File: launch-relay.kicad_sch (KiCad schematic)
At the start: 0 parts

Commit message: started schematic
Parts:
- added U1: (no value), RF_Module:BM78SPPS5XC2, symbol HPRC_Sensors:BMA580
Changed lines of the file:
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@@
 	(generator_version "10.0")
 	(paper "A4")
+	(symbol
+		(lib_id "HPRC_Sensors:BMA580")
+		(at 48.26 167.64 0)
+		(unit 1)
+		(body_style 1)
+		(exclude_from_sim no)
+		(in_bom yes)
+		(on_board yes)
+		(in_pos_files yes)
+		(dnp no)
+		(fields_autoplaced yes)
+		(property "Reference" "U1"
+			(at 48.26 157.48 0)
+			(show_name no)
+			(do_not_autoplace no)
+			(effects
+				(font
+					(size 1.27 1.27)
+				)
+			)
+		)
+		(property "Value" ""
+			(at 48.26 167.64 0)
+			(show_name no)
+			(do_not_autoplace no)
+			(effects
+				(font
+					(size 1.27 1.27)
+				)
+			)
+		)
+		(property "Footprint" "RF_Module:BM78SPPS5XC2"
+			(at 48.26 167.64 0)
+			(hide yes)
+			(show_name no)
+			(do_not_autoplace no)
+			(effects
+				(font
+					(size 1.27 1.27)
+				)
+			)
+		)
+		(property "Datasheet" ""
+			(at 48.26 167.64 0)
+			(hide yes)
+			(show_name no)
+			(do_not_autoplace no)
+			(effects
+				(font
+					(size 1.27 1.27)
+				)
+			)
+		)
+		(property "Description" ""
+			(at 48.26 167.64 0)
+			(hide yes)
+			(show_name no)
+			(do_not_autoplace no)
+			(effects
+				(font
+					(size 1.27 1.27)
+				)
+			)
+		)
+		(pin "1"
+		)
+		(pin "6"
+		)
+		(pin "4"
+		)
+		(pin "3"
+		)
+		(pin "2"
+		)
+		(pin "5"
+		)
+		(instances
+			(project "launch-relay"
+				(path "/5fd10500-b703-4d79-824f-0c6e126f5ac0"
+					(reference "U1")
+					(unit 1)
+				)
+			)
+		)
+	)
 	(sheet_instances
 		(path "/"

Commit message: started schematic
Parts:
- removed U1: (no value), RF_Module:BM78SPPS5XC2, symbol HPRC_Sensors:BMA580
- added BT1: BHSD-2032-PC, BHSD-2032-PC:BAT_BHSD-2032-PC, symbol BHSD-2032-PC:BHSD-2032-PC
- added C1: 100nF, symbol Device:C
- added D1, D2: LED, symbol Device:LED
- added J1: Conn_01x05_Pin, Package_DFN_QFN:QFN-20-1EP_5x5mm_P0.65mm_EP3.35x3.35mm, symbol Connector:Conn_01x05_Pin
- added R1, R2, R3, R4: 2.2k, symbol Device:R
- added U1: STM32U083KCUx, Package_DFN_QFN:QFN-32-1EP_5x5mm_P0.5mm_EP3.45x3.45mm, symbol MCU_ST_STM32U0:STM32U083KCUx
- added U3: (no value), RF_Module:BM78SPPS5XC2, symbol HPRC_Sensors:BMA580
- added U5: MX25R3235FM1IL0, SOP_8L_150_MAC, symbol MX25R3235FM1IL0:MX25R3235FM1IL0
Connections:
- new net: D1.2 (A), R3.2
- new net: D2.2 (A), R4.2
- new net +3V0: BT1.S+1, BT1.S+2, R1.2, R2.2, U1.1 (VDD), U1.17 (VDD), U1.5 (VDDA), U3.6 (VSS), U5.8 (VCC)
- new net BMA580_INT: U1.14 (PB0), U3.2 (INT)
- new net Battery_ADC: U1.9 (PA3)
- new net DEBUG_JTCK-SWCLK: U1.24 (PA14)
- new net DEBUG_JTCK_SWCLK: J1.1 (Pin_1)
- new net DEBUG_JTMS-SWDIO: J1.2 (Pin_2), U1.23 (PA13)
- new net DUMP: J1.5 (Pin_5), U1.18 (PA8)
- new net Flash_CS: U1.29 (PB6), U5.1 (CS#)
- new net GND: BT1.-, C1.1, U1.16 (VSS), U1.32 (VSS), U1.33 (VSS), U3.1 (VDD), U5.4 (GND)
- new net I2C2_SCL: R1.1, U1.13 (PA7), U3.5 (SCL)
- new net I2C2_SDA: R2.1, U1.12 (PA6), U3.4 (SDA)
- new net LED1: R4.1, U1.22 (PA12)
- new net LED2: R3.1, U1.21 (PA11)
- new net SPI3_MISO: U1.27 (PB4), U5.2 (SO/SIO1)
- new net SPI3_MOSI: U1.28 (PB5), U5.5 (SI/SIO0)
- new net SPI3_SCK: U1.26 (PB3), U5.6 (SCLK)
- new net Switch1: U1.7 (PA1)
- new net Switch2: U1.8 (PA2)
- new net USART1_RX: J1.3 (Pin_3), U1.20 (PA10)
- new net USART1_TX: J1.4 (Pin_4), U1.19 (PA9)
- new net VDD: U3.3 (INT2)
- no-connect marks 0 -> 9

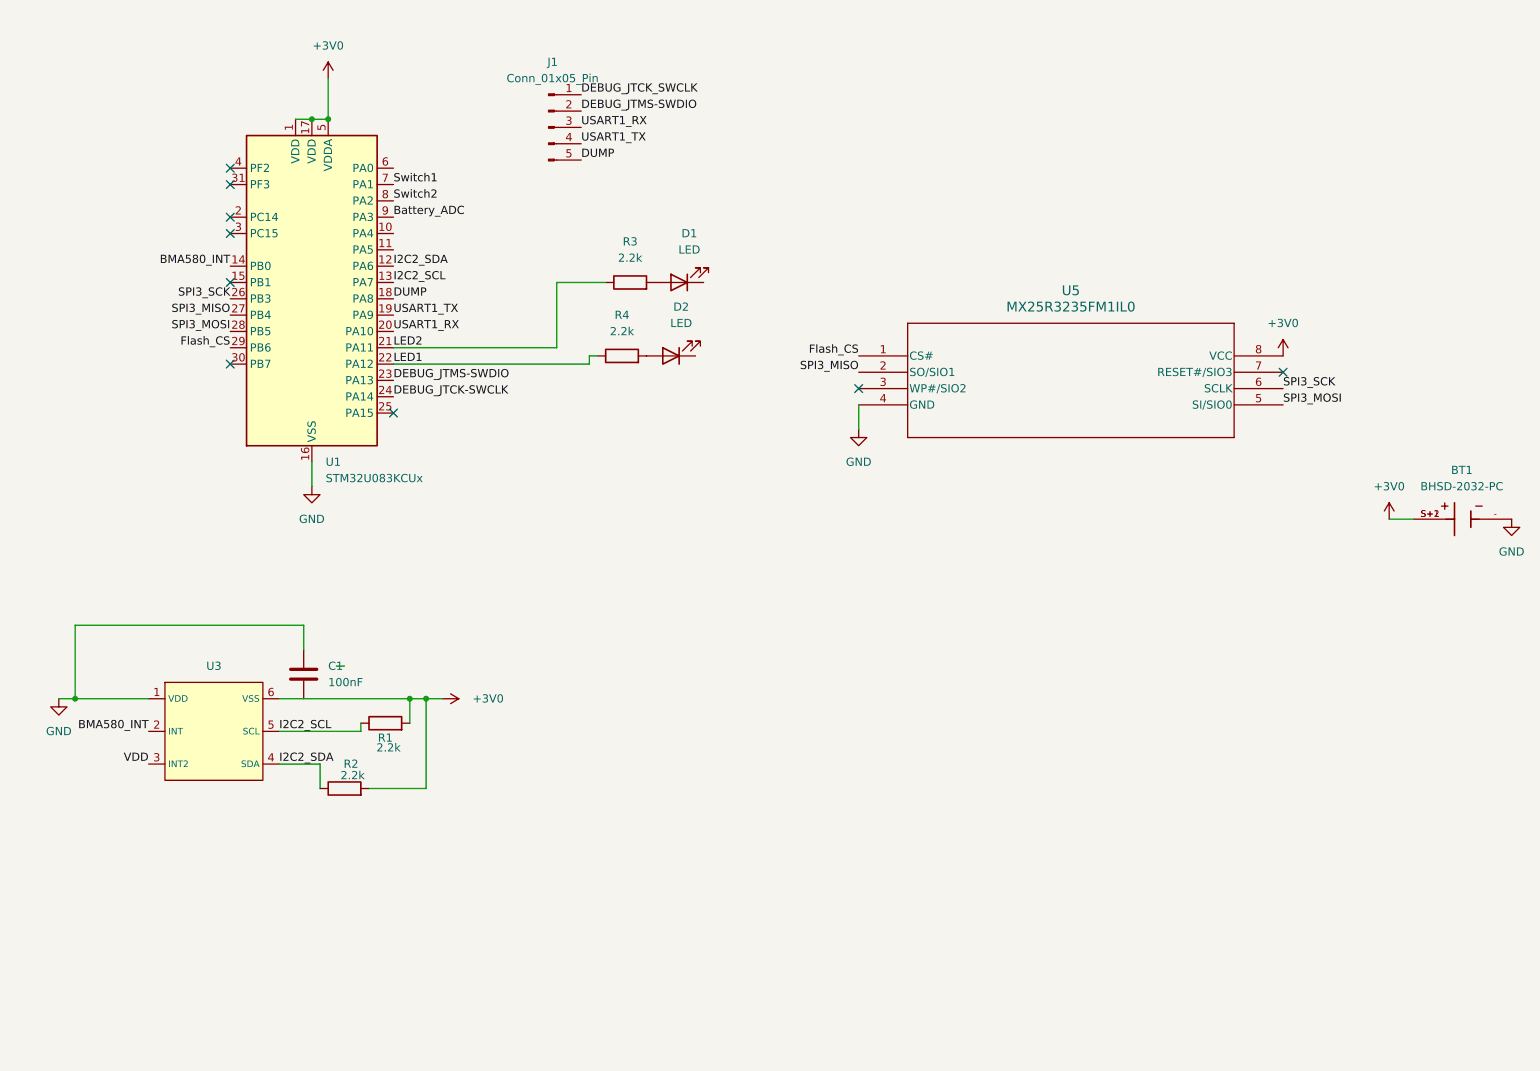
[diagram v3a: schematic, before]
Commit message: finalized schematic and prepped layout
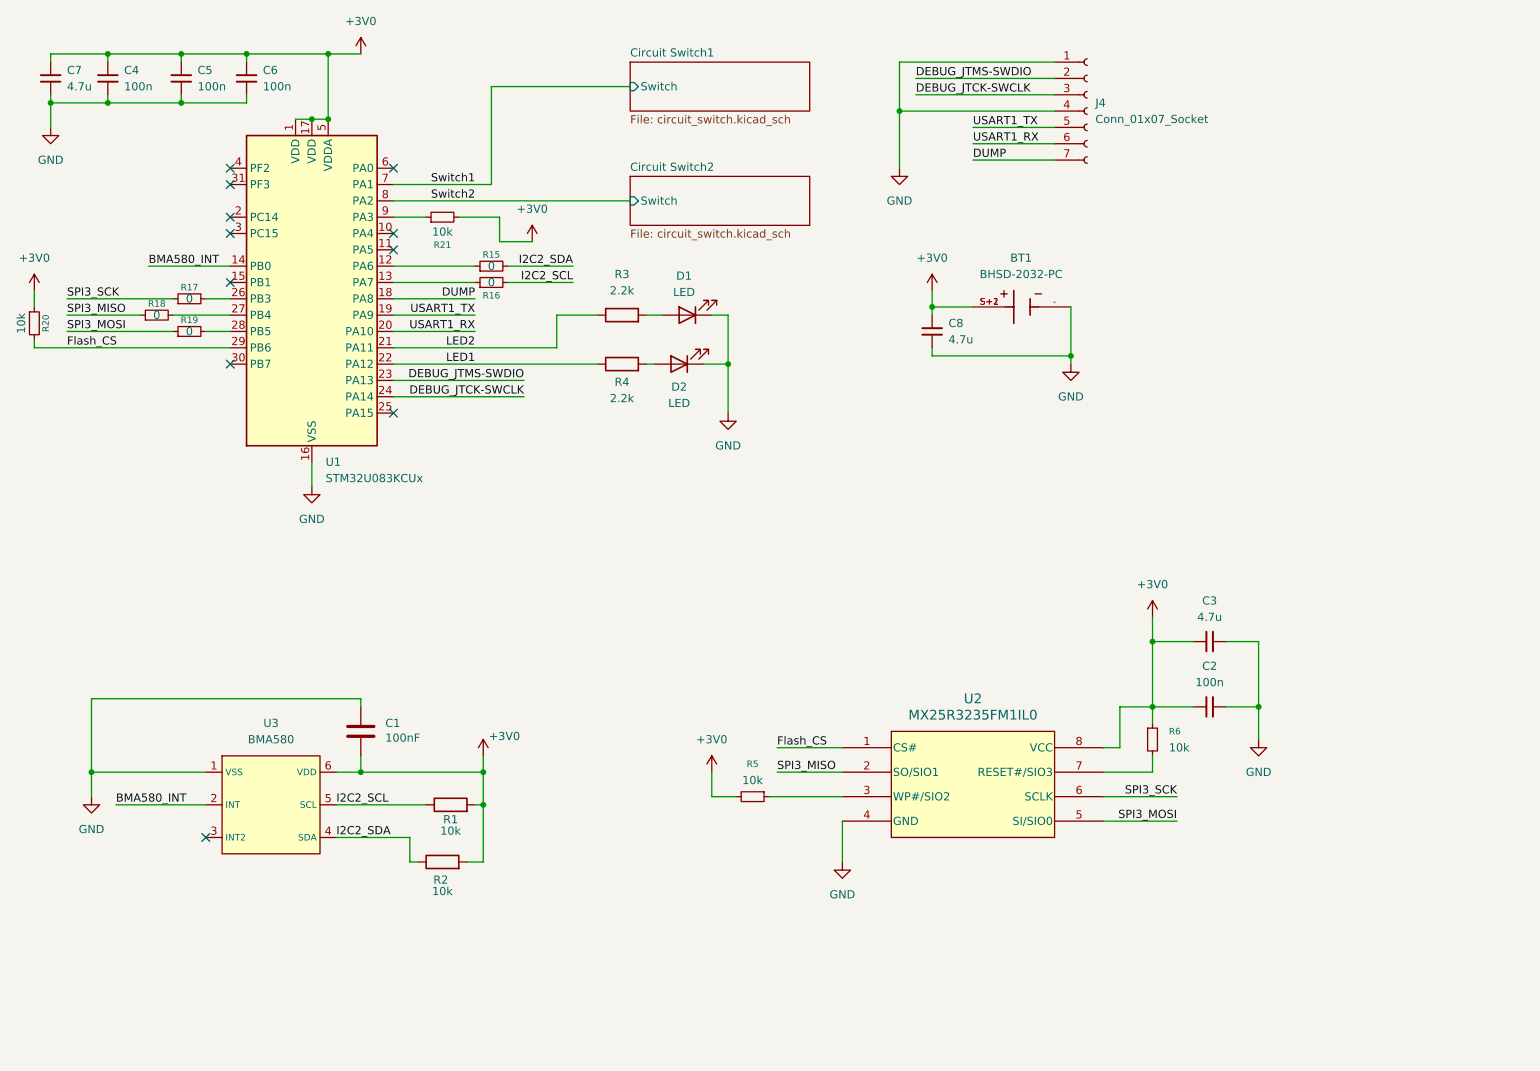
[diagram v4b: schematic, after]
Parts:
- removed J1: Conn_01x05_Pin, Package_DFN_QFN:QFN-20-1EP_5x5mm_P0.65mm_EP3.35x3.35mm, symbol Connector:Conn_01x05_Pin
- removed U5: MX25R3235FM1IL0, SOP_8L_150_MAC, symbol MX25R3235FM1IL0:MX25R3235FM1IL0
- added C2, C4, C5, C6: 100n, Capacitor_SMD:C_0603_1608Metric, symbol Device:C_Small
- added C3, C7, C8: 4.7u, Capacitor_SMD:C_0603_1608Metric, symbol Device:C_Small
- added J4: Conn_01x07_Socket, Connector_PinSocket_2.54mm:PinSocket_1x07_P2.54mm_Vertical, symbol Connector:Conn_01x07_Socket
- added R15, R16, R17, R18, R19: 0, Resistor_SMD:R_0603_1608Metric, symbol Device:R_Small
- added R20, R21, R5, R6: 10k, Resistor_SMD:R_0603_1608Metric, symbol Device:R_Small
- added U2: MX25R3235FM1IL0, HPRC_Storage:SOP_8L_150_MAC, symbol MX25R3235FM1IL0:MX25R3235FM1IL0
- BT1: footprint BHSD-2032-PC:BAT_BHSD-2032-PC -> HPRC_Connectors:BAT_BHSD-2032-PC
- C1: footprint (none) -> Capacitor_SMD:C_0603_1608Metric
- D1, D2: footprint (none) -> LED_SMD:LED_0805_2012Metric
- R1, R2: value 2.2k -> 10k; footprint (none) -> Resistor_SMD:R_0603_1608Metric
- R3, R4: footprint (none) -> Resistor_SMD:R_0603_1608Metric
- U3: value (none) -> BMA580; footprint RF_Module:BM78SPPS5XC2 -> HPRC_Sensors:BMA580
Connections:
- net +3V0: now also C1.2, C2.1, C3.1, C4.2, C5.2, C6.2, C7.2, C8.2, R20.1, R21.2, R5.2, R6.1, U2.8 (VCC)
- net DEBUG_JTCK-SWCLK: now also J4.3 (Pin_3)
- net DEBUG_JTMS-SWDIO: now also J4.2 (Pin_2)
- net DUMP: now also J4.7 (Pin_7)
- net Flash_CS: now also R20.2, U2.1 (CS#)
- net GND: now also D1.1 (K), D2.1 (K), C2.2, C3.2, C4.1, C5.1, C6.1, C7.1, C8.1, J4.1 (Pin_1), J4.4 (Pin_4), U2.4 (GND)
- net I2C2_SCL: now also R16.2; no longer U1.13 (PA7)
- net I2C2_SDA: now also R15.2; no longer U1.12 (PA6)
- net SPI3_MISO: now also R18.1, U2.2 (SO/SIO1); no longer U1.27 (PB4)
- net SPI3_MOSI: now also R19.1, U2.5 (SI/SIO0); no longer U1.28 (PB5)
- net SPI3_SCK: now also R17.1, U2.6 (SCLK); no longer U1.26 (PB3)
- net USART1_RX: now also J4.6 (Pin_6)
- net USART1_TX: now also J4.5 (Pin_5)
- net Battery_ADC: no longer names the net of U1.9 (PA3)
- net Battery_ADC: now also R21.1
- net VDD: no longer names the net of U3.3 (INT2)
- new net: R17.2, U1.26 (PB3)
- new net: R15.1, U1.12 (PA6)
- new net: R18.2, U1.27 (PB4)
- new net: R5.1, U2.3 (WP#/SIO2)
- new net: R6.2, U2.7 (RESET#/SIO3)
- new net: R19.2, U1.28 (PB5)
- new net: R16.1, U1.13 (PA7)
- no-connect marks 9 -> 11
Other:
- added sheet Circuit Switch1 (circuit_switch.kicad_sch)
- added sheet Circuit Switch2 (circuit_switch.kicad_sch)
- moved on the sheet: C1, D1, D2, R1, R2, R3, R4

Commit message: fixed switch circuit
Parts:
- added J1: Conn_01x02_Socket, Connector_PinSocket_2.54mm:PinSocket_1x02_P2.54mm_Vertical, symbol Connector:Conn_01x02_Socket
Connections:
- net +3V0: now also J1.1 (Pin_1); no longer BT1.S+1, BT1.S+2
- new net: BT1.S+1, BT1.S+2, J1.2 (Pin_2)
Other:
- moved on the sheet: BT1, C8
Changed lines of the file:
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@@
 	(paper "A4")
 	(junction
+		(at 167.64 59.69)
+		(diameter 0)
+		(color 0 0 0 0)
+	)
+	(junction
 		(at 85.09 135.89)
 		(diameter 0)
@@
 	)
 	(junction
-		(at 176.53 66.04)
+		(at 205.74 67.31)
 		(diameter 0)
 		(color 0 0 0 0)
@@
 	)
 	(junction
-		(at 154.94 58.42)
-		(diameter 0)
-		(color 0 0 0 0)
-	)
-	(junction
 		(at 149.86 27.94)
 		(diameter 0)
@@
 	(wire
 		(pts
-			(xy 66.04 128.27) (xy 66.04 130.81)
+			(xy 177.8 59.69) (xy 167.64 59.69)
 		)
 		(stroke
@@
 	(wire
 		(pts
-			(xy 96.52 64.77) (xy 96.52 59.69)
+			(xy 66.04 128.27) (xy 66.04 130.81)
 		)
 		(stroke
@@
 	(wire
 		(pts
-			(xy 83.82 57.15) (xy 71.12 57.15)
+			(xy 96.52 64.77) (xy 96.52 59.69)
 		)
 		(stroke
@@
 	(wire
 		(pts
-			(xy 71.12 64.77) (xy 96.52 64.77)
+			(xy 83.82 57.15) (xy 71.12 57.15)
 		)
 		(stroke
@@
 	(wire
 		(pts
-			(xy 26.67 25.4) (xy 26.67 26.67)
+			(xy 71.12 64.77) (xy 96.52 64.77)
 		)
 		(stroke
@@
 	(wire
 		(pts
-			(xy 154.94 55.88) (xy 154.94 58.42)
+			(xy 26.67 25.4) (xy 26.67 26.67)
 		)
 		(stroke
@@
 	(wire
 		(pts
-			(xy 92.71 48.26) (xy 87.63 48.26)
+			(xy 180.34 59.69) (xy 190.5 59.69)
 		)
 		(stroke
@@
 	(wire
 		(pts
-			(xy 154.94 58.42) (xy 161.29 58.42)
+			(xy 92.71 48.26) (xy 87.63 48.26)
 		)
 		(stroke
@@
 	(wire
 		(pts
-			(xy 154.94 64.77) (xy 154.94 66.04)
+			(xy 167.64 66.04) (xy 167.64 67.31)
 		)
 		(stroke
@@
 	(wire
 		(pts
-			(xy 176.53 66.04) (xy 176.53 58.42)
+			(xy 205.74 67.31) (xy 205.74 59.69)
 		)
 		(stroke
@@
 	(wire
 		(pts
-			(xy 154.94 59.69) (xy 154.94 58.42)
+			(xy 167.64 57.15) (xy 167.64 59.69)
 		)
 		(stroke
@@
 	(wire
 		(pts
-			(xy 176.53 67.31) (xy 176.53 66.04)
+			(xy 205.74 68.58) (xy 205.74 67.31)
 		)
 		(stroke
@@
 	(wire
 		(pts
+			(xy 177.8 58.42) (xy 177.8 59.69)
+		)
+		(stroke
+			(width 0)
+			(type default)
+		)
+	)
+	(wire
+		(pts
 			(xy 66.04 19.05) (xy 60.96 19.05)
 		)
@@
 	(wire
 		(pts
-			(xy 154.94 66.04) (xy 176.53 66.04)
+			(xy 167.64 67.31) (xy 205.74 67.31)
 		)
 		(stroke
@@
 	(wire
 		(pts
+			(xy 167.64 59.69) (xy 167.64 60.96)
+		)
+		(stroke
+			(width 0)
+			(type default)
+		)
+	)
+	(wire
+		(pts
 			(xy 41.91 62.23) (xy 45.72 62.23)
 		)
@@
 	(wire
 		(pts
+			(xy 180.34 58.42) (xy 180.34 59.69)
+		)
+		(stroke
+			(width 0)
+			(type default)
+		)
+	)
+	(wire
+		(pts
 			(xy 120.65 130.81) (xy 120.65 134.62)
 		)
@@
 	(symbol
 		(lib_id "power:+3V0")
-		(at 154.94 55.88 0)
+		(at 167.64 57.15 0)
 		(unit 1)
 		(body_style 1)
@@
 		(fields_autoplaced yes)
 		(property "Reference" "#PWR05"
-			(at 154.94 59.69 0)
+			(at 167.64 60.96 0)
 			(hide yes)
 			(show_name no)
@@
 		)
 		(property "Value" "+3V0"
-			(at 154.94 50.8 0)
+			(at 167.64 52.07 0)
 			(show_name no)
 			(do_not_autoplace no)
@@
 		)
 		(property "Footprint" ""
-			(at 154.94 55.88 0)
+			(at 167.64 57.15 0)
 			(hide yes)
 			(show_name no)
@@
 		)
 		(property "Datasheet" ""
-			(at 154.94 55.88 0)
+			(at 167.64 57.15 0)
 			(hide yes)
 			(show_name no)
@@
 		)
 		(property "Description" "Power symbol creates a global label with name \"+3V0\""
-			(at 154.94 55.88 0)
+			(at 167.64 57.15 0)
 			(hide yes)
 			(show_name no)
@@
 	)
 	(symbol
+		(lib_id "Connector:Conn_01x02_Socket")
+		(at 177.8 53.34 90)
+		(unit 1)
+		(body_style 1)
+		(exclude_from_sim no)
+		(in_bom yes)
+		(on_board yes)
+		(in_pos_files yes)
+		(dnp no)
+		(property "Reference" "J1"
+			(at 181.61 52.7049 90)
+			(show_name no)
+			(do_not_autoplace no)
+			(effects
+				(font
+					(size 1.27 1.27)
+				)
+				(justify right)
+			)
+		)
+		(property "Value" "Conn_01x02_Socket"
+			(at 173.736 49.784 90)
+			(show_name no)
+			(do_not_autoplace no)
+			(effects
+				(font
+					(size 1.27 1.27)
+				)
+				(justify right)
+			)
+		)
+		(property "Footprint" "Connector_PinSocket_2.54mm:PinSocket_1x02_P2.54mm_Vertical"
+			(at 177.8 53.34 0)
+			(hide yes)
+			(show_name no)
+			(do_not_autoplace no)
+			(effects
+				(font
+					(size 1.27 1.27)
+				)
+			)
+		)
+		(property "Datasheet" ""
+			(at 177.8 53.34 0)
+			(hide yes)
+			(show_name no)
+			(do_not_autoplace no)
+			(effects
+				(font
+					(size 1.27 1.27)
+				)
+			)
+		)
+		(property "Description" "Generic connector, single row, 01x02, script generated"
+			(at 177.8 53.34 0)
+			(hide yes)
+			(show_name no)
+			(do_not_autoplace no)
+			(effects
+				(font
+					(size 1.27 1.27)
+				)
+			)
+		)
+		(pin "2"
+		)
+		(pin "1"
+		)
+		(instances
+			(project "launch-relay"
+				(path "/5fd10500-b703-4d79-824f-0c6e126f5ac0"
+					(reference "J1")
+					(unit 1)
+				)
+			)
+		)
+	)
+	(symbol
 		(lib_id "power:+3V0")
 		(at 15.24 55.88 0)
@@
 	(symbol
 		(lib_id "BHSD-2032-PC:BHSD-2032-PC")
-		(at 168.91 58.42 0)
+		(at 198.12 59.69 0)
 		(unit 1)
 		(body_style 1)
@@
 		(in_pos_files yes)
 		(dnp no)
-		(fields_autoplaced yes)
 		(property "Reference" "BT1"
-			(at 168.783 50.8 0)
+			(at 198.12 55.626 0)
 			(show_name no)
 			(do_not_autoplace no)
@@
 		)
 		(property "Value" "BHSD-2032-PC"
-			(at 168.783 53.34 0)
+			(at 197.612 63.5 0)
 			(show_name no)
 			(do_not_autoplace no)
@@
 		)
 		(property "Footprint" "HPRC_Connectors:BAT_BHSD-2032-PC"
-			(at 168.91 58.42 0)
+			(at 198.12 59.69 0)
 			(hide yes)
 			(show_name no)
@@
 		)
 		(property "Datasheet" ""
-			(at 168.91 58.42 0)
+			(at 198.12 59.69 0)
 			(hide yes)
 			(show_name no)
@@
 		)
 		(property "Description" ""
-			(at 168.91 58.42 0)
+			(at 198.12 59.69 0)
 			(hide yes)
 			(show_name no)
@@
 		)
 		(property "PARTREV" "K"
-			(at 168.91 58.42 0)
+			(at 198.12 59.69 0)
 			(hide yes)
 			(show_name no)
@@
 		)
 		(property "STANDARD" "Manufacturer Recommendations"
-			(at 168.91 58.42 0)
+			(at 198.12 59.69 0)
 			(hide yes)
 			(show_name no)
@@
 		)
 		(property "MAXIMUM_PACKAGE_HEIGHT" "4.75 mm"
-			(at 168.91 58.42 0)
+			(at 198.12 59.69 0)
 			(hide yes)
 			(show_name no)
@@
 		)
 		(property "MANUFACTURER" "MPD"
-			(at 168.91 58.42 0)
+			(at 198.12 59.69 0)
 			(hide yes)
 			(show_name no)
@@
 	(symbol
 		(lib_id "Device:C_Small")
-		(at 154.94 62.23 180)
+		(at 167.64 63.5 180)
 		(unit 1)
 		(body_style 1)
@@
 		(fields_autoplaced yes)
 		(property "Reference" "C8"
-			(at 157.48 60.9599 0)
+			(at 170.18 62.2299 0)
 			(show_name no)
 			(do_not_autoplace no)
@@
 		)
 		(property "Value" "4.7u"
-			(at 157.48 63.4999 0)
+			(at 170.18 64.7699 0)
 			(show_name no)
 			(do_not_autoplace no)
@@
 		)
 		(property "Footprint" "Capacitor_SMD:C_0603_1608Metric"
-			(at 154.94 62.23 0)
+			(at 167.64 63.5 0)
 			(hide yes)
 			(show_name no)
@@
 		)
 		(property "Datasheet" ""
-			(at 154.94 62.23 0)
+			(at 167.64 63.5 0)
 			(hide yes)
 			(show_name no)
@@
 		)
 		(property "Description" "Unpolarized capacitor, small symbol"
-			(at 154.94 52.07 0)
+			(at 167.64 53.34 0)
 			(hide yes)
 			(show_name no)
@@
 	(symbol
 		(lib_id "power:GND")
-		(at 176.53 67.31 0)
+		(at 205.74 68.58 0)
 		(unit 1)
 		(body_style 1)
@@
 		(fields_autoplaced yes)
 		(property "Reference" "#PWR01"
-			(at 176.53 73.66 0)
+			(at 205.74 74.93 0)
 			(hide yes)
 			(show_name no)
@@
 		)
 		(property "Value" "GND"
-			(at 176.53 72.39 0)
+			(at 205.74 73.66 0)
 			(show_name no)
 			(do_not_autoplace no)
@@
 		)
 		(property "Footprint" ""
-			(at 176.53 67.31 0)
+			(at 205.74 68.58 0)
 			(hide yes)
 			(show_name no)
@@
 		)
 		(property "Datasheet" ""
-			(at 176.53 67.31 0)
+			(at 205.74 68.58 0)
 			(hide yes)
 			(show_name no)
@@
 		)
 		(property "Description" "Power symbol creates a global label with name \"GND\" , ground"
-			(at 176.53 67.31 0)
+			(at 205.74 68.58 0)
 			(hide yes)
 			(show_name no)

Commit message: ready to review
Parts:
- removed R18: 0, Resistor_SMD:R_0603_1608Metric, symbol Device:R_Small
- C1: renamed from C7; footprint Capacitor_SMD:C_0603_1608Metric -> Capacitor_SMD:C_0402_1005Metric
- C2: renamed from C4; footprint Capacitor_SMD:C_0603_1608Metric -> Capacitor_SMD:C_0402_1005Metric
- C3: renamed from C5; footprint Capacitor_SMD:C_0603_1608Metric -> Capacitor_SMD:C_0402_1005Metric
- C4: renamed from C6; footprint Capacitor_SMD:C_0603_1608Metric -> Capacitor_SMD:C_0402_1005Metric
- C5: renamed from C1; footprint Capacitor_SMD:C_0603_1608Metric -> Capacitor_SMD:C_0402_1005Metric
- C6: renamed from C8; footprint Capacitor_SMD:C_0603_1608Metric -> Capacitor_SMD:C_0402_1005Metric
- C7: renamed from C3; footprint Capacitor_SMD:C_0603_1608Metric -> Capacitor_SMD:C_0402_1005Metric
- C8: renamed from C2; footprint Capacitor_SMD:C_0603_1608Metric -> Capacitor_SMD:C_0402_1005Metric
- R1: renamed from R20; footprint Resistor_SMD:R_0603_1608Metric -> Resistor_SMD:R_0402_1005Metric
- R10: renamed from R4; footprint Resistor_SMD:R_0603_1608Metric -> Resistor_SMD:R_0402_1005Metric
- R11: renamed from R5; footprint Resistor_SMD:R_0603_1608Metric -> Resistor_SMD:R_0402_1005Metric
- R12: renamed from R6; footprint Resistor_SMD:R_0603_1608Metric -> Resistor_SMD:R_0402_1005Metric
- R2: renamed from R17; footprint Resistor_SMD:R_0603_1608Metric -> Resistor_SMD:R_0402_1005Metric
- R3: renamed from R19; footprint Resistor_SMD:R_0603_1608Metric -> Resistor_SMD:R_0402_1005Metric
- R4: renamed from R21; footprint Resistor_SMD:R_0603_1608Metric -> Resistor_SMD:R_0402_1005Metric
- R5: renamed from R2; value 10k -> 4.7k; footprint Resistor_SMD:R_0603_1608Metric -> Resistor_SMD:R_0402_1005Metric
- R6: renamed from R1; value 10k -> 4.7k; footprint Resistor_SMD:R_0603_1608Metric -> Resistor_SMD:R_0402_1005Metric
- R7: renamed from R15; footprint Resistor_SMD:R_0603_1608Metric -> Resistor_SMD:R_0402_1005Metric
- R8: renamed from R16; footprint Resistor_SMD:R_0603_1608Metric -> Resistor_SMD:R_0402_1005Metric
- R9: renamed from R3; footprint Resistor_SMD:R_0603_1608Metric -> Resistor_SMD:R_0402_1005Metric
- renumbered D2 to D1, D1 to D2, J4 to J2, U3 to U1, U1 to U2, U2 to U3
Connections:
- net SPI3_MISO: now also U2.27 (PB4)
